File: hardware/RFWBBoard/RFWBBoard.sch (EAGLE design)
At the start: 55 parts, among them IC1 24LC025ST, J1 CON-71742-2184-BOT, M1 MOUNT-HOLE3.3, M2 MOUNT-HOLE3.3, M3 MOUNT-HOLE3.3, M4 MOUNT-HOLE3.3, U1 MAX2830IPC-7351, U2 LDB212G4010C-001, U3 LDB212G4010C-001, X1 LTI-SASF54GT, X2 LTI-SASF54GT, X3 LTI-SASF54GT, X4 LTI-SASF54GT

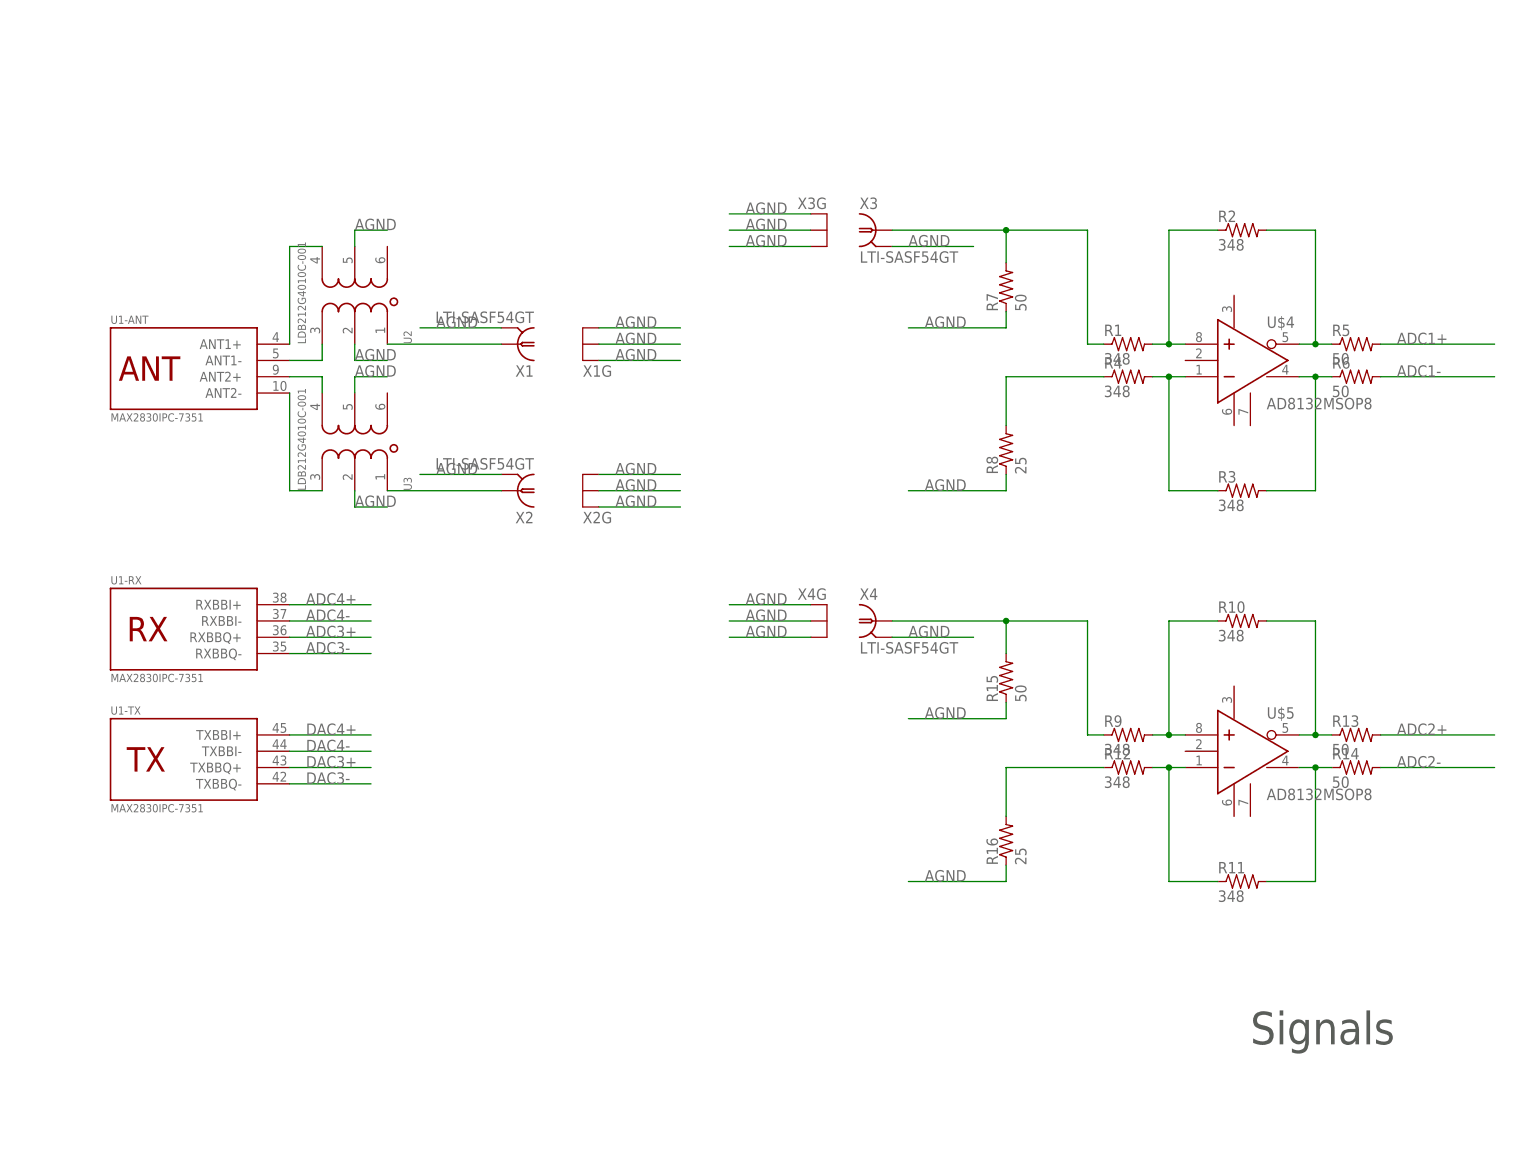
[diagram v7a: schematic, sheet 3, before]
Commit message: - Matched impedance wires for antennas (14 mil -> 50 Ohm) - Baseband for DAC and DAC
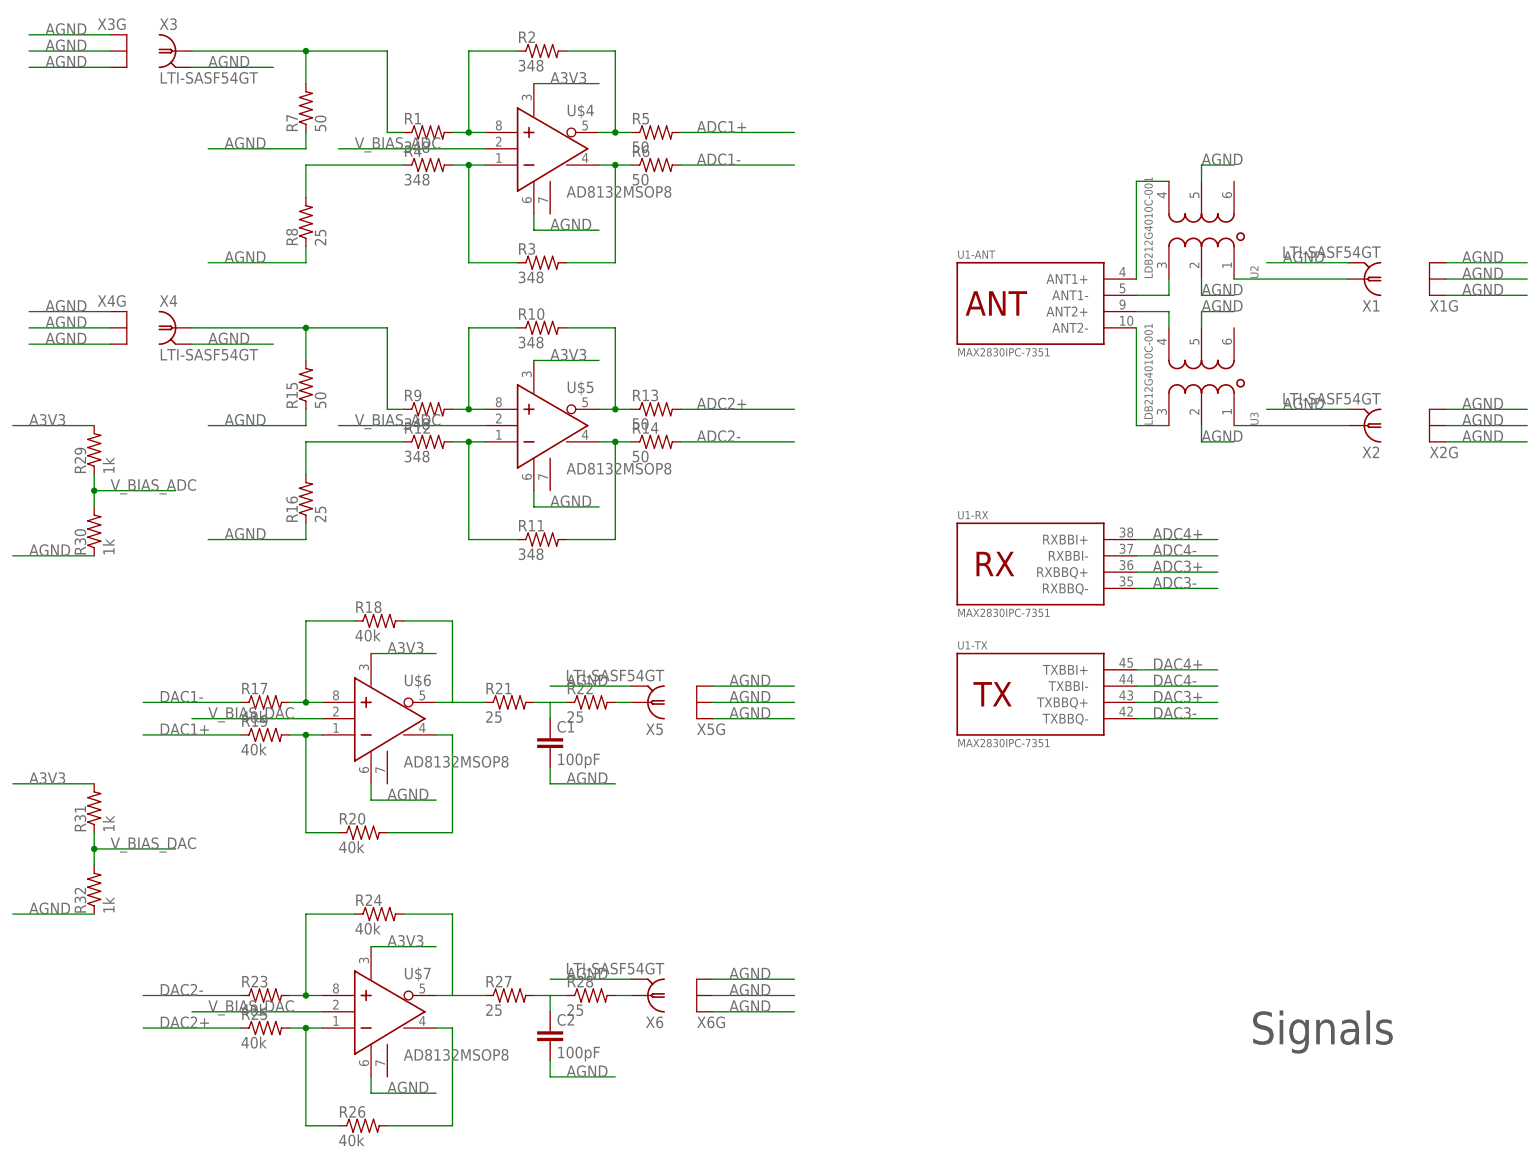
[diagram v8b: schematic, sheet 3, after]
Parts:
- added C1, C2: 100pF, RFWBBoard:C0402
- added R17, R18, R19, R20, R23, R24, R25, R26: 40k, RFWBBoard:R0402
- added R21, R22, R27, R28: 25, RFWBBoard:R0402
- added R29, R30, R31, R32: 1k, RFWBBoard:R0402
- added U$6, U$7: AD8132MSOP8, RFWBBoard:AD8132MSOP8
- added X5, X6: LTI-SASF54GT, RFWBBoard:LTI-SASF54GT
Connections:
- new net N$23: R17.2, R18.1, U$6.+IN
- new net N$24: R19.2, R20.1, U$6.-IN
- new net N$25: R18.2, R21.1, U$6.-OUT
- new net N$26: R20.2, U$6.+OUT
- new net N$27: C1.1, R21.2, R22.1
- new net N$28: R23.2, R24.1, U$7.+IN
- new net N$29: R22.2, X5G$1.1
- new net N$30: R25.2, R26.1, U$7.-IN
- new net N$31: R24.2, R27.1, U$7.-OUT
- new net N$32: R26.2, U$7.+OUT
- new net N$33: C2.1, R27.2, R28.1
- new net N$34: R28.2, X6G$1.1
- new net V_BIAS_ADC: R29.1, R30.2, U$4.V_OCM, U$5.V_OCM
- new net V_BIAS_DAC: R31.1, R32.2, U$6.V_OCM, U$7.V_OCM
- net A3V3: now also R29.2, R31.2, U$4.V_S+, U$5.V_S+, U$6.V_S+, U$7.V_S+
- net AGND: now also C1.2, C2.2, R30.1, R32.1, U$4.V_S-, U$5.V_S-, U$6.V_S-, U$7.V_S-, X5G$1.GND, X5G.GND@1, X5G.GND@2, X5G.GND@3, X6G$1.GND, X6G.GND@1, X6G.GND@2, X6G.GND@3
- net DAC1+: now also R19.1
- net DAC1-: now also R17.1
- net DAC2+: now also R25.1
- net DAC2-: now also R23.1
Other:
- moved on the sheet: R1, R10, R11, R12, R13, R14, R15, R16, R2, R3, R4, R5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
